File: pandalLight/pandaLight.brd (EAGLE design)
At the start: 83 x 57.4 mm, 126 parts, among them J1 PJ-037A, U1 MIC2230-XXYML, U10 TPD12S016PWR, U11 PAN1322, U2 6SLX9TQG144, U3 93LC46BT-I/OT, U4 FT2232HL, U5 TPD12S016PWR, U6 20Mhz, U7 TXB0104RGYR, U8 TPD12S016PWR, U9 M25P40-VMN, X1 USBUB-S, X2 HDMI_RECEPTICAL_A, X3 HDMI_RECEPTICAL_A, X4 HDMI_RECEPTICAL_A, X5 PMOD-2X6, X6 PMOD-2X6, Y1 403

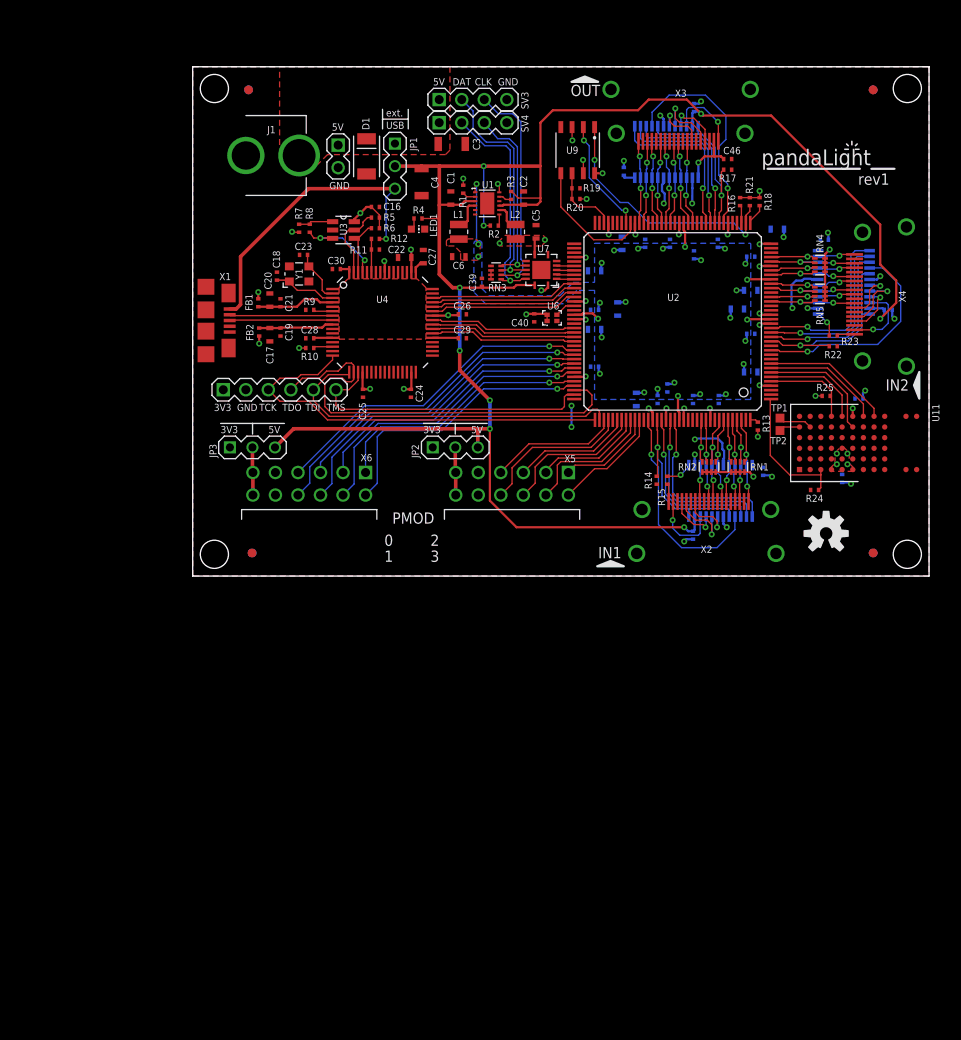
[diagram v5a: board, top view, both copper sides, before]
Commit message: Changed buck regulator and level translator to SOT packages, yet unrouted
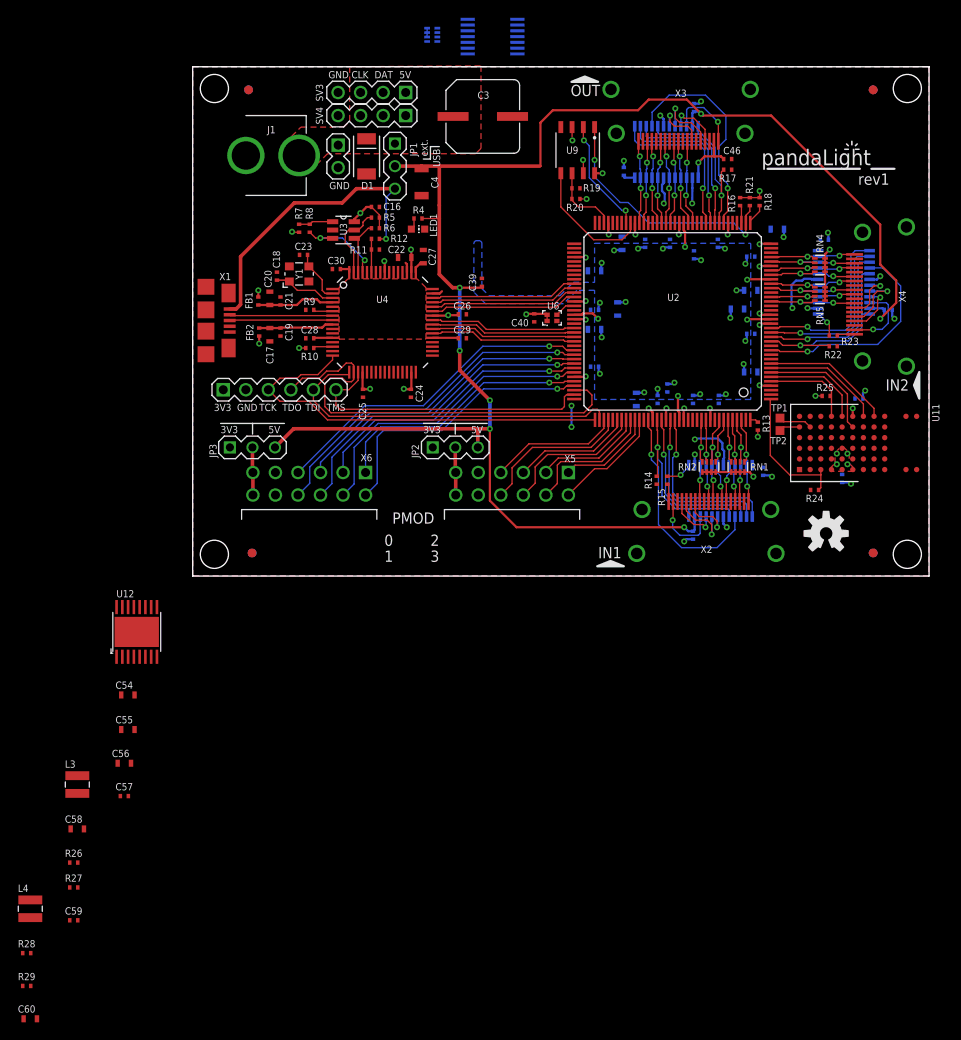
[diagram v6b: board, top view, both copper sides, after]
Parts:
- removed C1, C2: 4.7u, pandaLight:C0603
- removed C5, C6: 10u, pandaLight:C0603
- removed L1, L2: 2.2u, 1.3A, pandaLight:VLS-E_1008
- removed R1, R2, R3: 100k, pandaLight:R0402
- removed U1: MIC2230-XXYML, pandaLight:MLF-12
- added C54, C55: 10u, pandaLight:C0603
- added C56: 4.7u, pandaLight:C0603
- added C57, C59: 0.1u, pandaLight:C0402
- added C58, C60: 22u, pandaLight:C0603
- added L3: 2.2u, 1.3A, pandaLight:SRN3015_3X3
- added L4: 1.5u, 1.3, pandaLight:SRN3015_3X3
- added R26: 73.2, pandaLight:R0402
- added R27, R29: 22.1, pandaLight:R0402
- added R28: 12.7, pandaLight:R0402
- added U12: TPS542941PWP, pandaLight:R-PDSO-G16
- C3: value 100u -> 1000u; device pandaLight:C1206 -> pandaLight:MVY_HA0
- U7: value TXB0104RGYR -> TXB0104PWR; device pandaLight:S-PVQFN-N14 -> pandaLight:R-PDSO-G14
- moved RN3 27.8 mm to (27.0, 61.0), flipped to the bottom, turned to 90 degrees
- moved U7 26.9 mm to (33.8, 60.8), flipped to the bottom
- moved SV3 11.4 mm to (20.2, 54.5), turned to 180 degrees
- moved SV4 11.4 mm to (20.2, 51.9), turned to 180 degrees
- moved C3 4.68 mm to (32.7, 51.8), turned to 90 degrees
- moved C20 0.20 mm to (8.70, 31.3)
- moved C21 0.20 mm to (9.90, 31.0)
- moved FB1 0.20 mm to (7.40, 31.0)
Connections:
- removed net N$25: R3.2, U1.11
- removed net N$27: R1.2, U1.2
- removed net N$4: R2.2, U1.7
- removed net SW1: L2.1, U1.8
- removed net SW2: L1.1, U1.4
- new net N$14: C57.1, U12.2
- new net N$15: R26.1, U12.7
- new net N$16: C59.1, U12.15
- new net N$17: C58.2, U12.4
- new net N$18: C59.2, L4.1, U12.14
- new net N$20: R28.1, U12.10
- new net N$21: C60.2, U12.13
- new net N$3: C57.2, L3.1, U12.3
- new net VREG5: C56.1, U12.9
- net +1V2: now also C60.1, L4.2, R28.2, R29.1; no longer C6.1, L1.2, U1.1
- net +3V3: now also C58.1, L3.2, R26.2, R27.1, U12.12; no longer C5.1, L2.2, R1.1, U1.12
- net +5V: now also C54.1, C55.1, U12.1, U12.16, U12.5; no longer C1.1, C2.1, R2.1, R3.1, U1.3, U1.9
- net GND: now also C54.2, C55.2, C56.2, R27.2, R29.2, U12.8; no longer C1.2, C2.2, C5.2, C6.2, U1.5, U1.6, U1.EP, U7.EP
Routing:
- net +5V: track 213.2 -> 183.0 mm, vias 9 -> 7
- net LEDS1_DATA_5V: track 26.0 -> 0.00 mm, vias 1 -> 0
- net LEDS1_CLK_5V: track 25.7 -> 0.00 mm, vias 1 -> 0
- net LEDS0_DATA_5V: track 24.9 -> 0.00 mm, vias 1 -> 0
- net LEDS0_CLK_5V: track 21.1 -> 0.00 mm, vias 1 -> 0
- net +1V2: track 21.9 -> 14.0 mm, vias 8 -> 5
- net +3V3: track 75.2 -> 70.4 mm, vias 47 -> 42
- net SW2: track 3.64 -> 0.00 mm
- net SW1: track 3.08 -> 0.00 mm
- net GND: track 54.4 -> 56.8 mm
- net LEDS1_DATA: track 2.00 -> 0.00 mm
- net LEDS1_CLK: track 2.00 -> 0.00 mm
- net LEDS0_DATA: track 2.00 -> 0.00 mm
- net LEDS0_CLK: track 2.00 -> 0.00 mm
- net N$27: track 1.51 -> 0.00 mm
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- removed copper zone on layer 1, net +1V2

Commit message: Routed new buck regulator
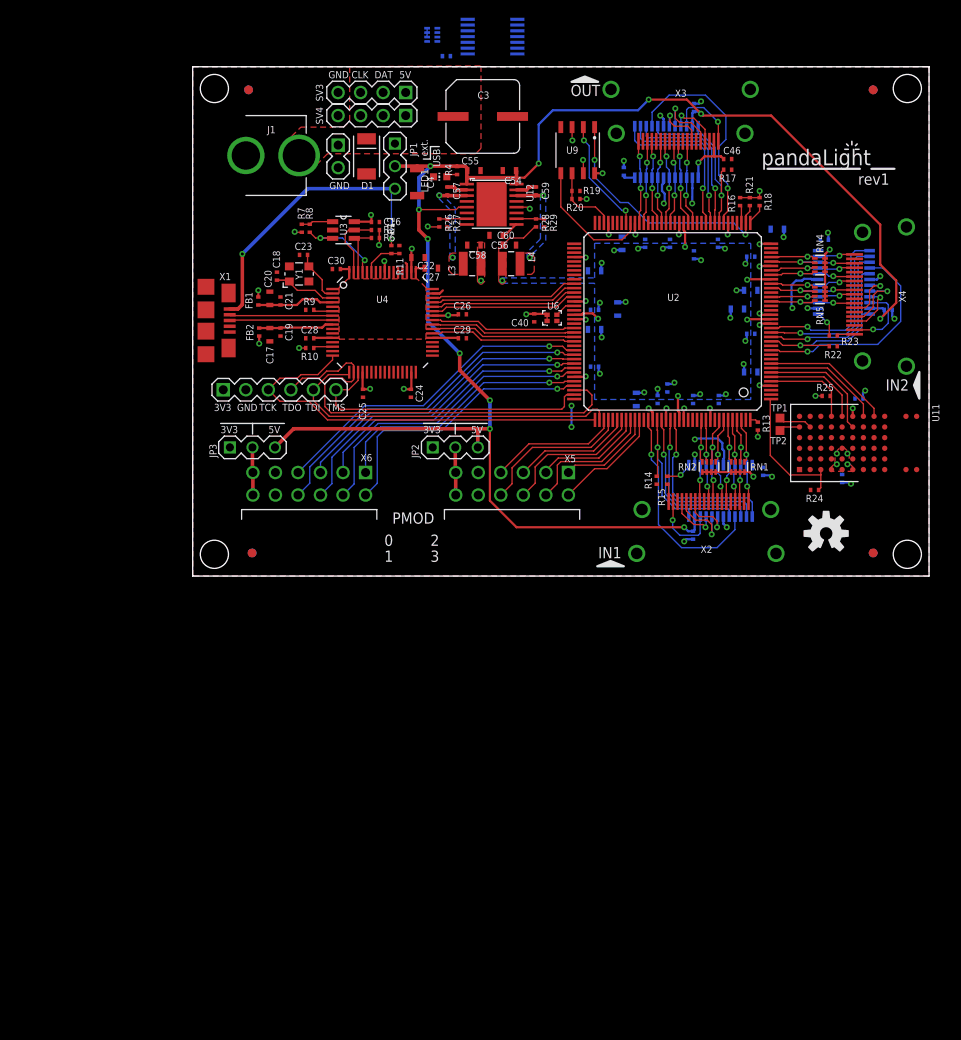
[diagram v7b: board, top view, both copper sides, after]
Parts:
- moved R29 103.9 mm to (39.6, 39.8), turned to 270 degrees
- moved C60 102.6 mm to (35.7, 37.3)
- moved R28 100.3 mm to (38.7, 39.8), turned to 270 degrees
- moved C59 97.3 mm to (38.7, 43.4), turned to 270 degrees
- moved L4 90.7 mm to (35.9, 35.2), turned to 270 degrees
- moved R27 85.9 mm to (28.7, 39.8), turned to 270 degrees
- moved R26 83.0 mm to (27.8, 39.8), turned to 270 degrees
- moved C58 79.5 mm to (31.7, 37.3), turned to 180 degrees
- moved C57 77.3 mm to (28.7, 43.4), turned to 270 degrees
- moved C55 74.1 mm to (31.7, 45.7)
- moved L3 73.7 mm to (31.5, 35.2), turned to 90 degrees
- moved C54 73.1 mm to (35.7, 45.7), turned to 180 degrees
- moved C56 72.8 mm to (34.2, 38.4), turned to 180 degrees
- moved U12 62.6 mm to (33.7, 41.9), turned to 270 degrees
- moved C39 25.8 mm to (28.6, 58.6), flipped to the bottom, turned to 0 degrees
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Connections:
- removed net N$17: C58.2, U12.4
- removed net N$20 (its old number): R28.1, U12.10
- removed net N$21: C60.2, U12.13
- new net N$4: R26.1, R27.1, U12.7
- net +1V2: no longer R29.1
- net +3V3: no longer R27.1
- net GND: now also C58.2, C60.2, U12.13, U12.4
- net N$15: now also R28.1, R29.1, U12.10; no longer R26.1, U12.7
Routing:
- net +5V: track 183.0 -> 188.5 mm, vias 7 -> 11
- net +1V2: track 14.0 -> 18.4 mm, vias 5 -> 6
- net N$3: track 0.00 -> 3.22 mm, vias 0 -> 2
- net N$20: track 0.00 -> 3.12 mm, vias 0 -> 2
- net N$15: track 0.00 -> 3.11 mm
- net N$4: track 0.00 -> 3.11 mm
- net +3V3: track 70.4 -> 73.2 mm, vias 42 -> 46
- net N$16: track 0.00 -> 2.33 mm
- net N$14: track 0.00 -> 2.33 mm
- net VREG5: track 0.00 -> 2.06 mm
- net USB_PWRSAVE#: track 3.77 -> 4.63 mm
- net N$6: track 8.70 -> 7.88 mm
- net USB_VBUS: track 34.2 -> 34.0 mm, vias 1 -> 2
- added copper zone on layer 1, net +1V2
- added copper zone on layer 1, net N$20
- added copper zone on layer 16, net N$20
- added copper zone on layer 1, net N$3
- added copper zone on layer 16, net N$3

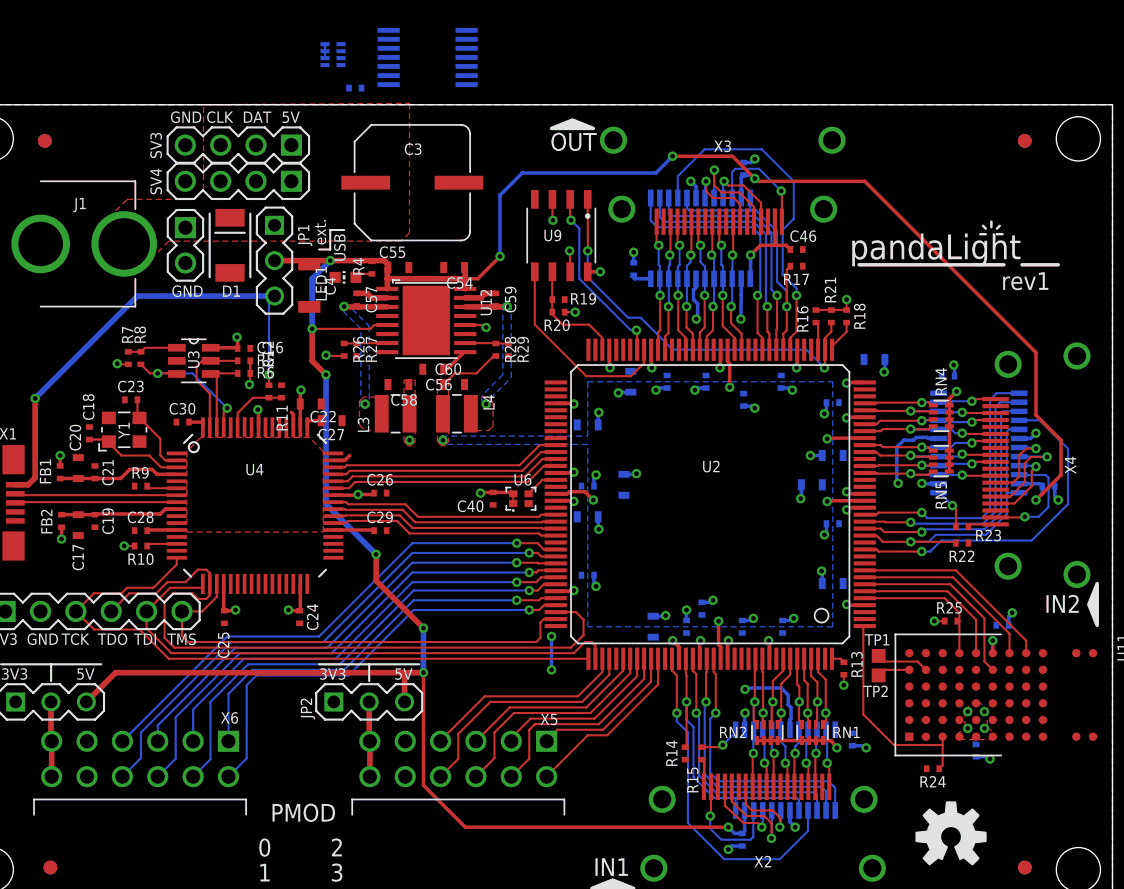
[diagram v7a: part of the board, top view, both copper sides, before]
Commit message: Routed everything, corrected unconnected ground pins (due to higher isolation)
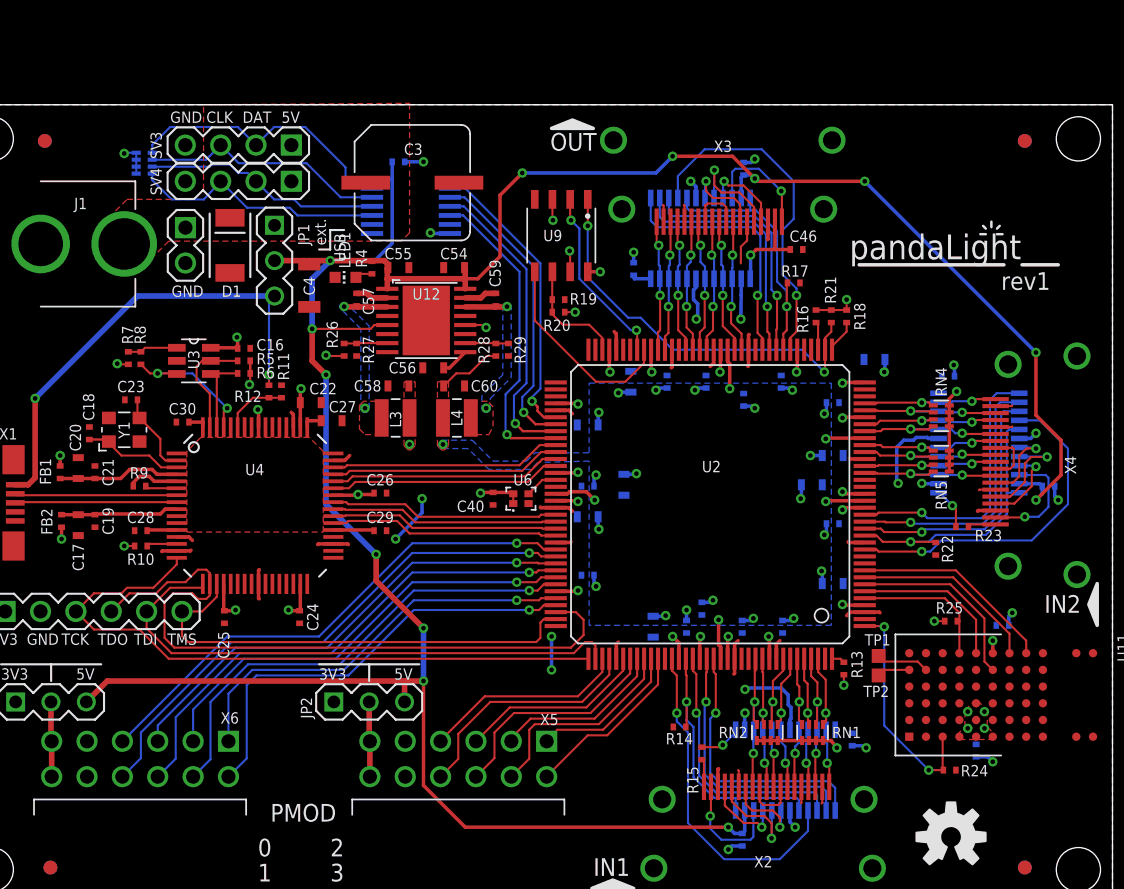
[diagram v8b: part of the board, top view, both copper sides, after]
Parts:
- moved RN3 15.6 mm to (13.4, 53.2)
- moved U7 10.8 mm to (32.6, 50.1)
- moved C39 6.14 mm to (31.7, 53.3), turned to 180 degrees
- moved R22 1.94 mm to (70.3, 25.5), turned to 90 degrees
- moved R14 1.94 mm to (51.9, 12.7), turned to 0 degrees
- moved R17 1.22 mm to (60.1, 44.6)
- moved R24 1.20 mm to (71.3, 9.60), turned to 180 degrees
- moved L3 0.30 mm to (31.5, 34.9)
- moved L4 0.30 mm to (35.9, 34.9)
- moved C22 0.10 mm to (25.4, 36.0)
- moved C56 0.10 mm to (34.2, 38.5)
- moved R9 0.10 mm to (13.1, 30.0)
- moved C58 0.10 mm to (31.7, 37.2)
- moved C60 0.10 mm to (35.7, 37.2)
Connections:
- net LEDS0_CLK: now also U7.2; no longer U7.5
- net LEDS0_DATA: now also U7.5; no longer U7.2
- net LEDS0_DATA_5V: now also RN3.7, U7.11; no longer RN3.5, U7.13
- net LEDS1_CLK: now also U7.4; no longer U7.3
- net LEDS1_DATA: now also U7.3; no longer U7.4
- net LEDS1_DATA_5V: now also RN3.5, U7.13; no longer RN3.7, U7.11
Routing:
- net GND: track 56.9 -> 126.4 mm, vias 40 -> 45
- net LEDS0_DATA: track 0.00 -> 22.4 mm, vias 0 -> 1
- net LEDS1_CLK: track 0.00 -> 22.0 mm, vias 0 -> 1
- net LEDS1_DATA: track 0.00 -> 21.6 mm, vias 0 -> 1
- net LEDS0_CLK: track 0.00 -> 21.2 mm, vias 0 -> 1
- net LEDS1_DATA_5V: track 0.00 -> 20.3 mm
- net LEDS0_CLK_5V: track 0.00 -> 18.4 mm
- net LEDS1_CLK_5V: track 0.00 -> 17.8 mm
- net LEDS0_DATA_5V: track 0.00 -> 17.1 mm
- net +5V: track 188.5 -> 199.9 mm, vias 11 -> 13
- net +3V3: track 73.2 -> 78.4 mm
- net HDMI_RX1_EN: track 22.3 -> 20.8 mm
- net HDMI_RX0_EN: track 21.9 -> 20.5 mm
- net HDMI_TX_CTRL_EN: track 20.7 -> 19.4 mm
- net BT_RESET#: track 15.4 -> 16.5 mm, vias 0 -> 2
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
